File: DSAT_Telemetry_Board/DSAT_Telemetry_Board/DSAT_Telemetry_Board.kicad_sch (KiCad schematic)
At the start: 1 part

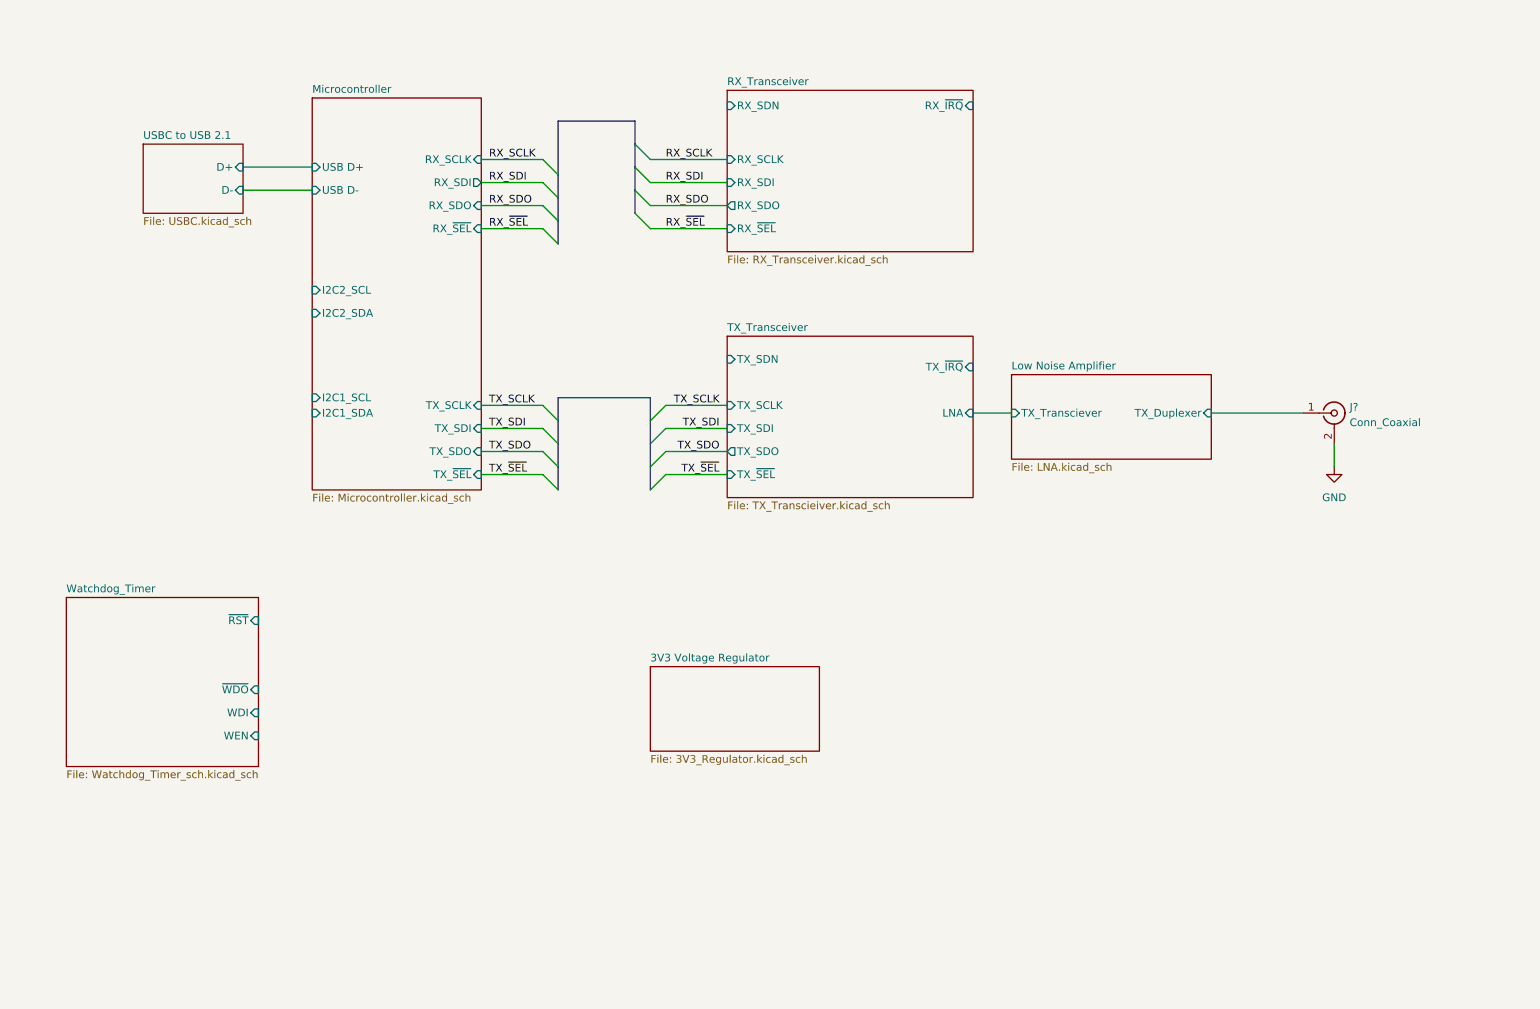
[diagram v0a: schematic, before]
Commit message: Added Transciever Updates/Biases/RF_Switch
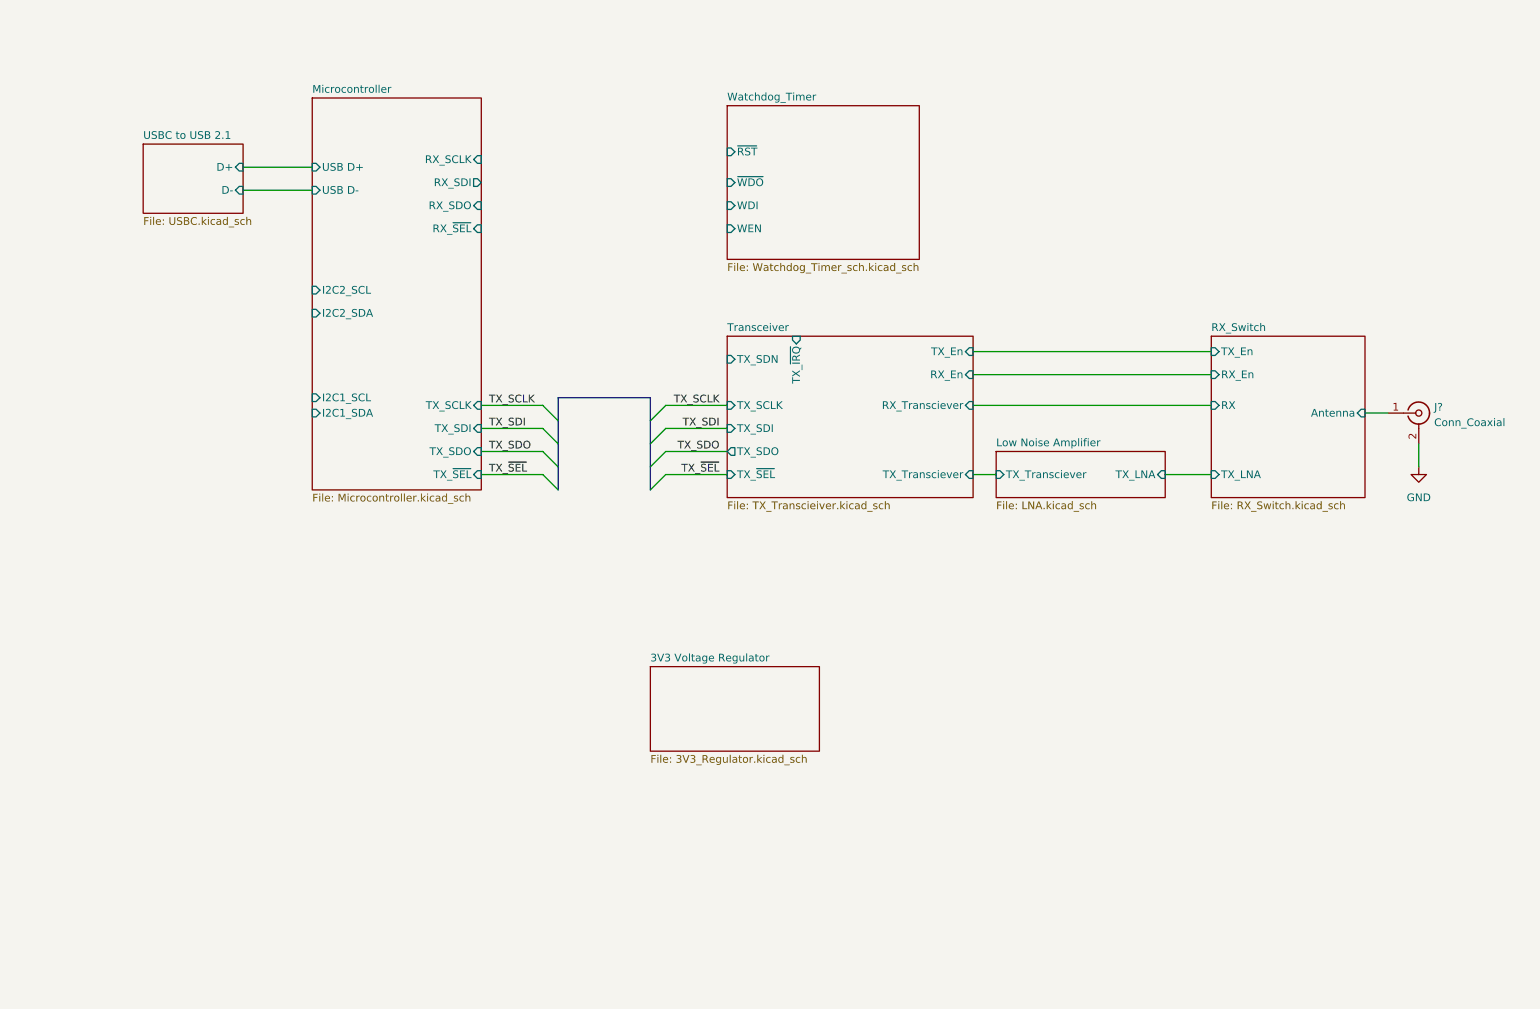
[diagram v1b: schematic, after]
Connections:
- net Low Noise Amplifier/TX_Duplexer renamed RX_Switch/Antenna
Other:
- sheet TX_Transceiver renamed Transceiver
- removed sheet RX_Transceiver
- added sheet RX_Switch (RX_Switch.kicad_sch)
- sheet Low Noise Amplifier ports: added TX_LNA; removed TX_Duplexer
- sheet Transceiver ports: added RX_En, RX_Transciever, TX_En, TX_Transciever; removed LNA
- moved on the sheet: J?

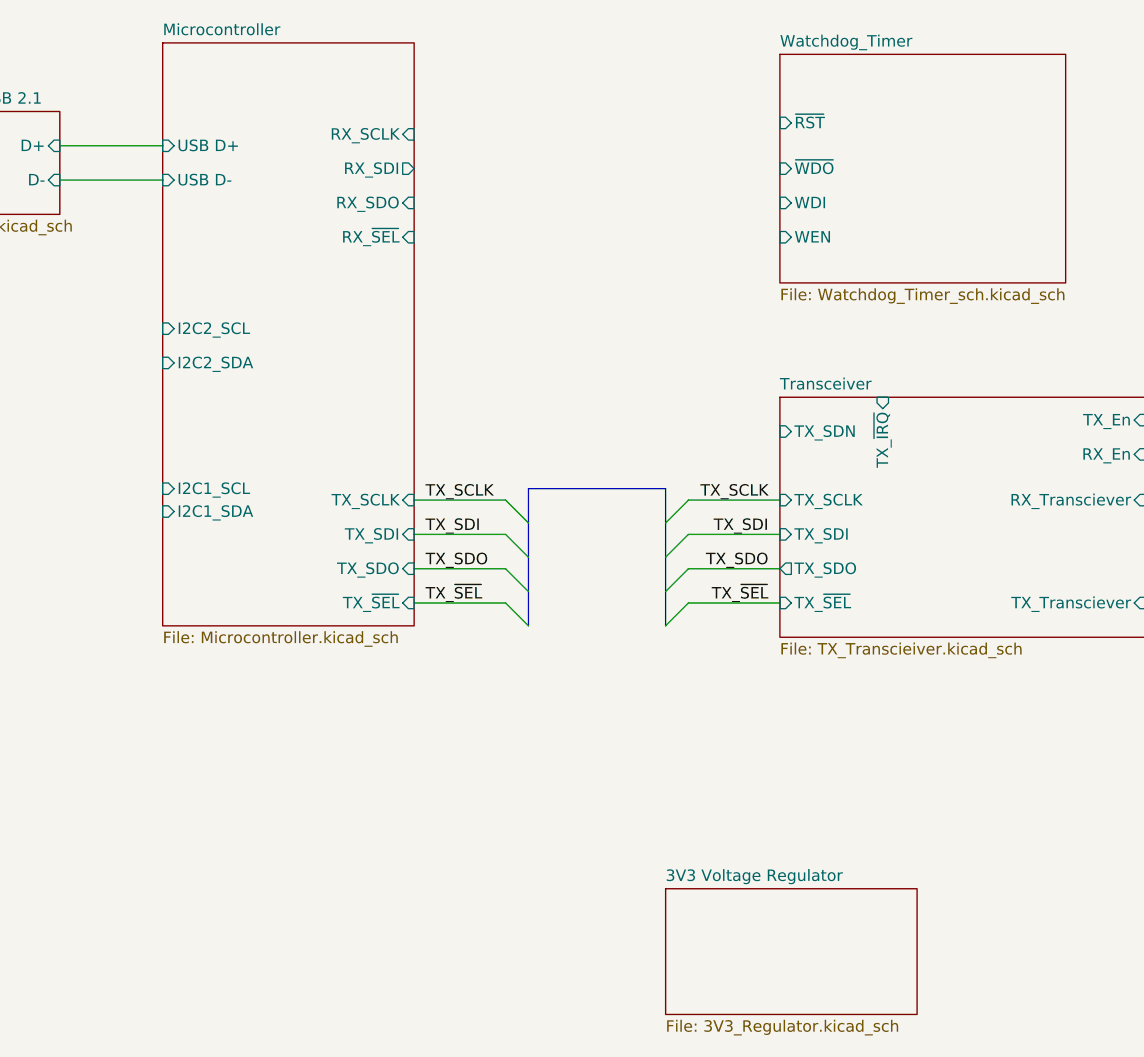
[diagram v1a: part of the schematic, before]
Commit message: Added Matching Networks/Linear Regulator/Watchdog Pins
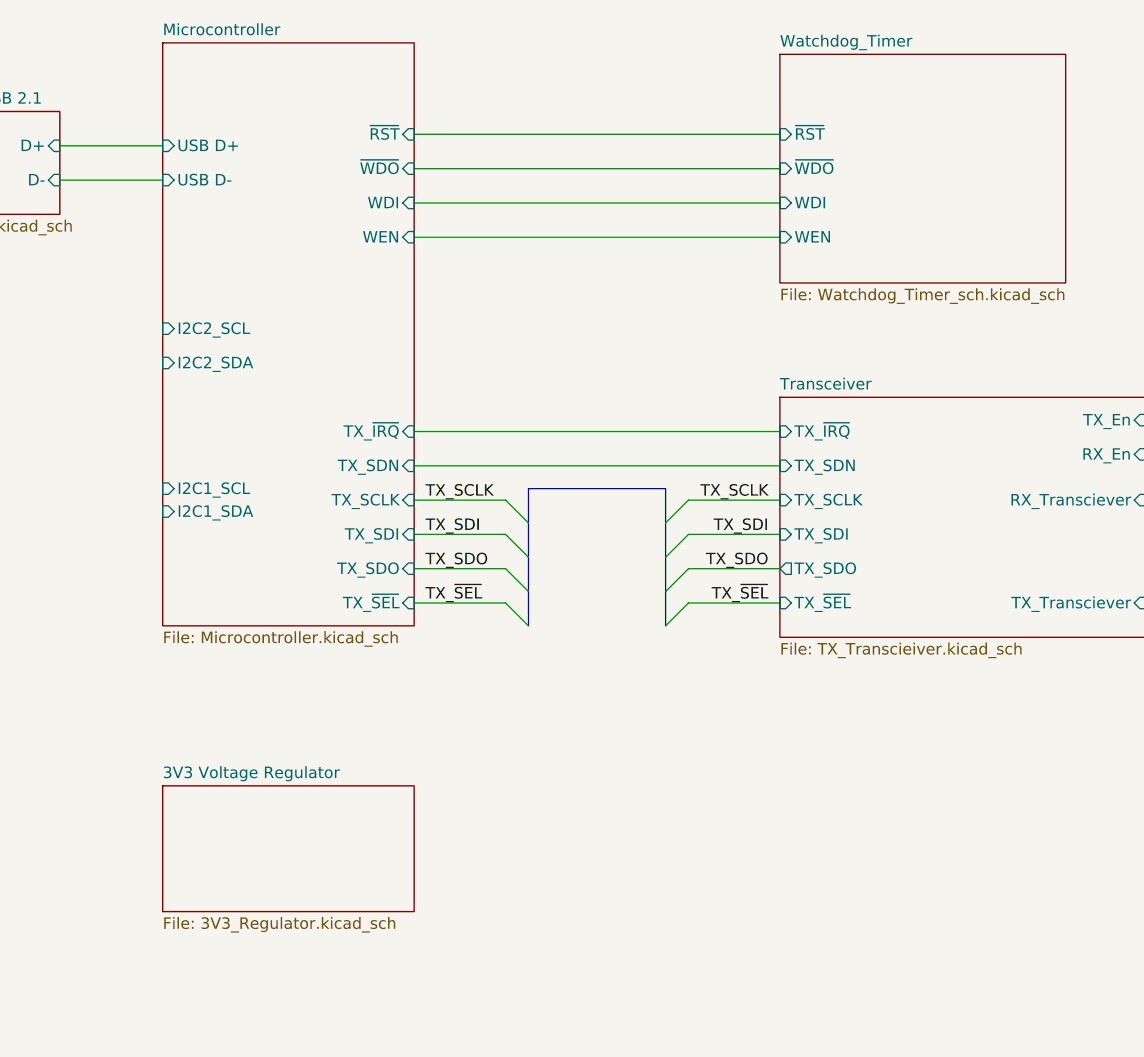
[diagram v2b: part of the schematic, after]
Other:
- sheet Microcontroller ports: added TX_SDN, TX_~{IRQ}, WDI, WEN, ~{RST}, ~{WDO}; removed RX_SCLK, RX_SDI, RX_SDO, RX_~{SEL}

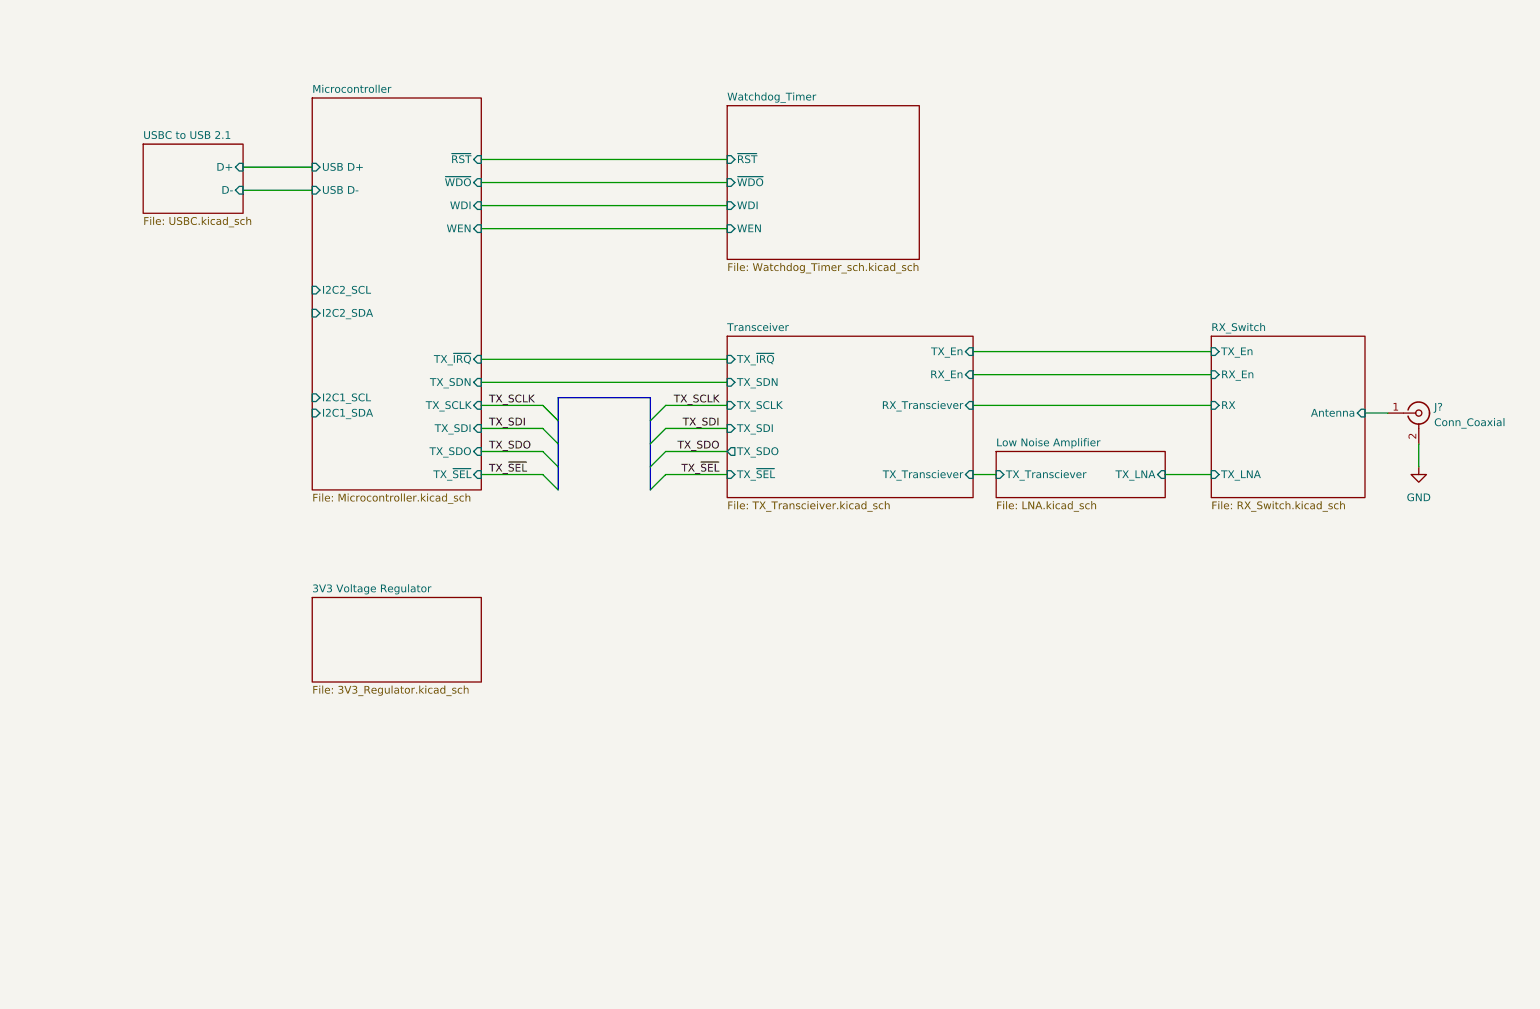
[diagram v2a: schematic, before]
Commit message: Added Test Points
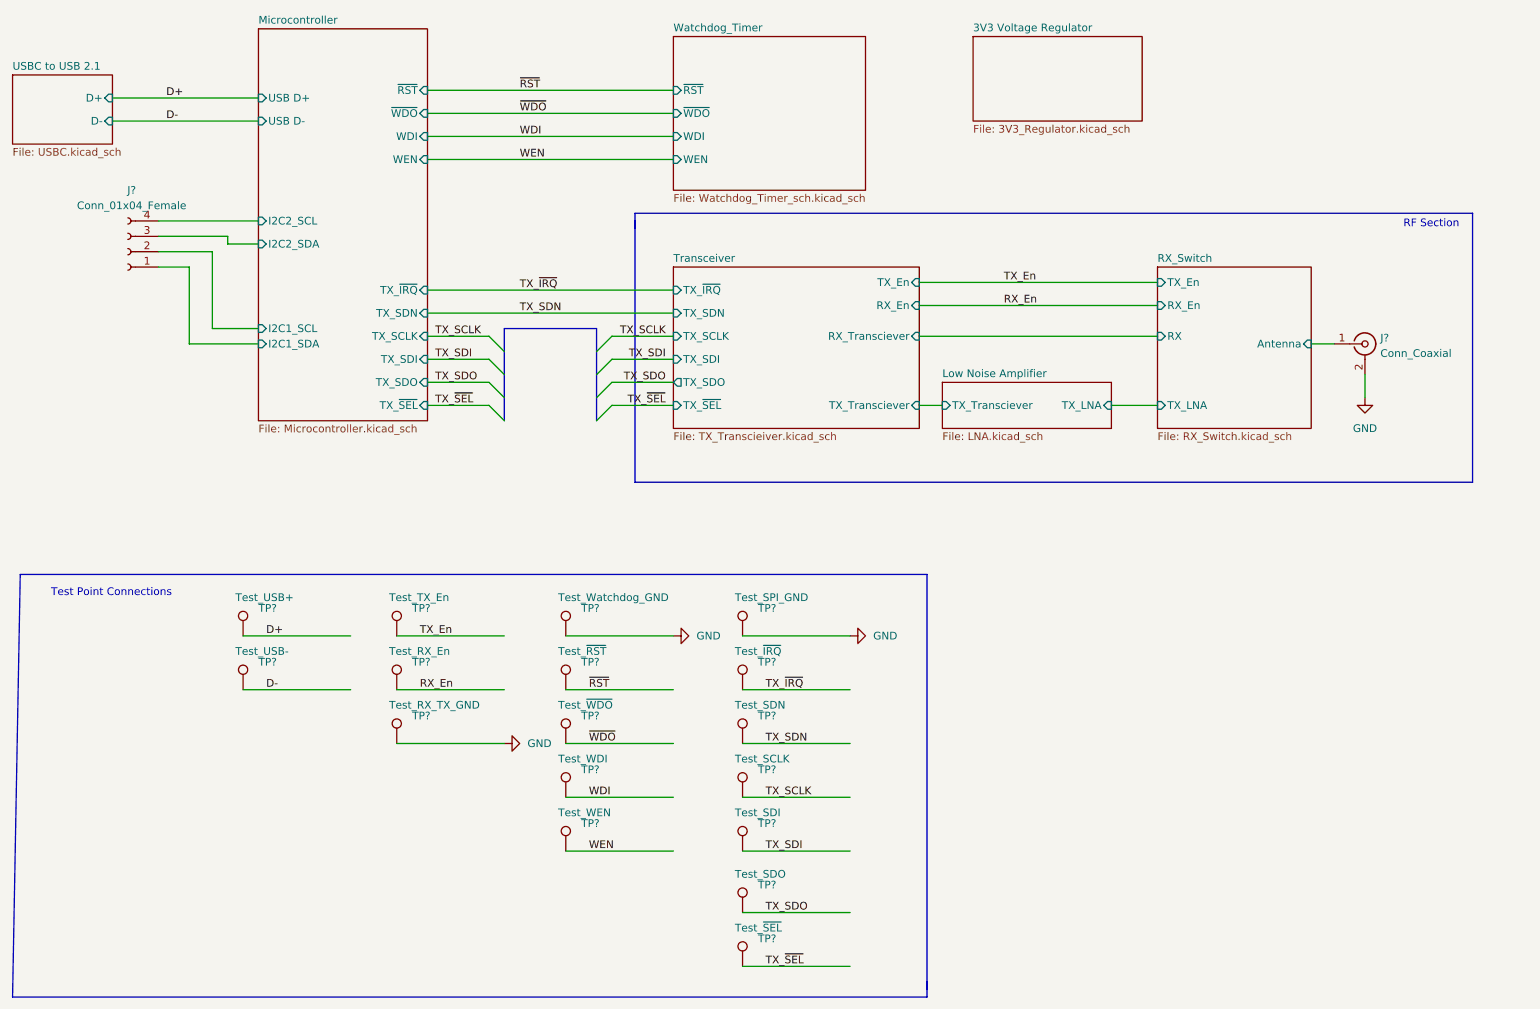
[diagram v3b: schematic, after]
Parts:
- added J?: Conn_01x04_Female, Connector_PinHeader_2.54mm:PinHeader_1x04_P2.54mm_Vertical, symbol Connector:Conn_01x04_Female
- added TP?: Test_SDN, TestPoint:TestPoint_Pad_D2.5mm, symbol Connector:TestPoint
- added TP?: Test_~{RST}, TestPoint:TestPoint_Pad_D2.5mm, symbol Connector:TestPoint
- added TP?: Test_USB-, TestPoint:TestPoint_Pad_D2.5mm, symbol Connector:TestPoint
- added TP?: Test_~{WDO}, TestPoint:TestPoint_Pad_D2.5mm, symbol Connector:TestPoint
- added TP?: Test_~{SEL}, TestPoint:TestPoint_Pad_D2.5mm, symbol Connector:TestPoint
- added TP?: Test_USB+, TestPoint:TestPoint_Pad_D2.5mm, symbol Connector:TestPoint
- added TP?: Test_RX_TX_GND, TestPoint:TestPoint_Pad_D2.5mm, symbol Connector:TestPoint
- added TP?: Test_SPI_GND, TestPoint:TestPoint_Pad_D2.5mm, symbol Connector:TestPoint
- added TP?: Test_SDI, TestPoint:TestPoint_Pad_D2.5mm, symbol Connector:TestPoint
- added TP?: Test_WEN, TestPoint:TestPoint_Pad_D2.5mm, symbol Connector:TestPoint
- added TP?: Test_Watchdog_GND, TestPoint:TestPoint_Pad_D2.5mm, symbol Connector:TestPoint
- added TP?: Test_SCLK, TestPoint:TestPoint_Pad_D2.5mm, symbol Connector:TestPoint
- added TP?: Test_WDI, TestPoint:TestPoint_Pad_D2.5mm, symbol Connector:TestPoint
- added TP?: Test_TX_En, TestPoint:TestPoint_Pad_D2.5mm, symbol Connector:TestPoint
- added TP?: Test_RX_En, TestPoint:TestPoint_Pad_D2.5mm, symbol Connector:TestPoint
- added TP?: Test_~{IRQ}, TestPoint:TestPoint_Pad_D2.5mm, symbol Connector:TestPoint
- added TP?: Test_SDO, TestPoint:TestPoint_Pad_D2.5mm, symbol Connector:TestPoint
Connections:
- net GND: now also TP?.1, TP?.1, TP?.1
- net Microcontroller/I2C1_SCL: now also J?.2 (Pin_2)
- net Microcontroller/I2C1_SDA: now also J?.1 (Pin_1)
- net Microcontroller/I2C2_SCL: now also J?.4 (Pin_4)
- net Microcontroller/I2C2_SDA: now also J?.3 (Pin_3)
- net TX_SCLK: now also TP?.1
- net TX_SDI: now also TP?.1
- net TX_SDO: now also TP?.1
- net TX_~{SEL}: now also TP?.1
- new net D+: TP?.1
- new net D-: TP?.1
- new net RX_En: TP?.1
- new net TX_En: TP?.1
- new net TX_SDN: TP?.1
- new net TX_~{IRQ}: TP?.1
- new net WDI: TP?.1
- new net WEN: TP?.1
- new net ~{RST}: TP?.1
- new net ~{WDO}: TP?.1
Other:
- note added: "RF Section"
- note added: "Test Point Connections"
- moved on the sheet: J?
